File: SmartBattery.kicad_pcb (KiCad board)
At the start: 4 copper layers, 100 x 80 mm, 433 parts, among them J1 USB_C_Receptacle_USB2.0, J10 JST 2P-1.0, J11 JST 2P-1.0, J12 Conn_02x05_Odd_Even, J13 Conn_01x03_Male, J15 USB_C_Receptacle_USB2.0, J2 ST-USB-003A, J3 JACK-C-PC-10A-RA(R), J4 JST 2P-1.0, J5 JST 2P-1.0, J6 JST 2P-1.0, J7 JST 2P-1.0, J8 JST 2P-1.0, J9 JST 2P-1.0, Q1 VBA2625, Q10 AON7400A, Q11 AON7400A, Q12 BSC067N06LS3, Q13 BSC067N06LS3, Q14 2n7002K, Q15 VBA2625, Q16 VBA2625, Q17 VBA2625, Q18 VBA2625, Q19 VBA2625, Q2 2n7002K, Q20 VBA2625, Q21 2n7002K, Q22 AO3401A, Q23 VBA2625, Q24 VBA2625, Q25 2n7002K, Q26 VBA2625, Q27 VBA2625, Q3 AON7400A, Q4 AON7400A, Q5 AON7400A, Q6 AON7400A, Q7 2n7002K, Q8 AON7400A, Q9 AON7400A, SW1 SW_Push, SW2 SW_Push, SW3 SW_Push, SW4 SW_Push, U1 BQ25703ARSNR, U10 ESP32-WROOM-32U, U11 STUSB4500, U12 STUSB4700, U13 TPS2511DGNR, U14 HT7533-1, U15 LMR14030SDDAR, U2 BQ294706DSGR, U3 ITV4030, U4 BQ40Z50, U5 LM5175PWPR, U6 STM32F730R8T6, U7 LY68L6400SLIT, U8 LMR14030SDDAR, U9 FS35ND01G-S1Y2QWFI000, Y1 Q13FC1350000400, Y2 Crystal_GND24

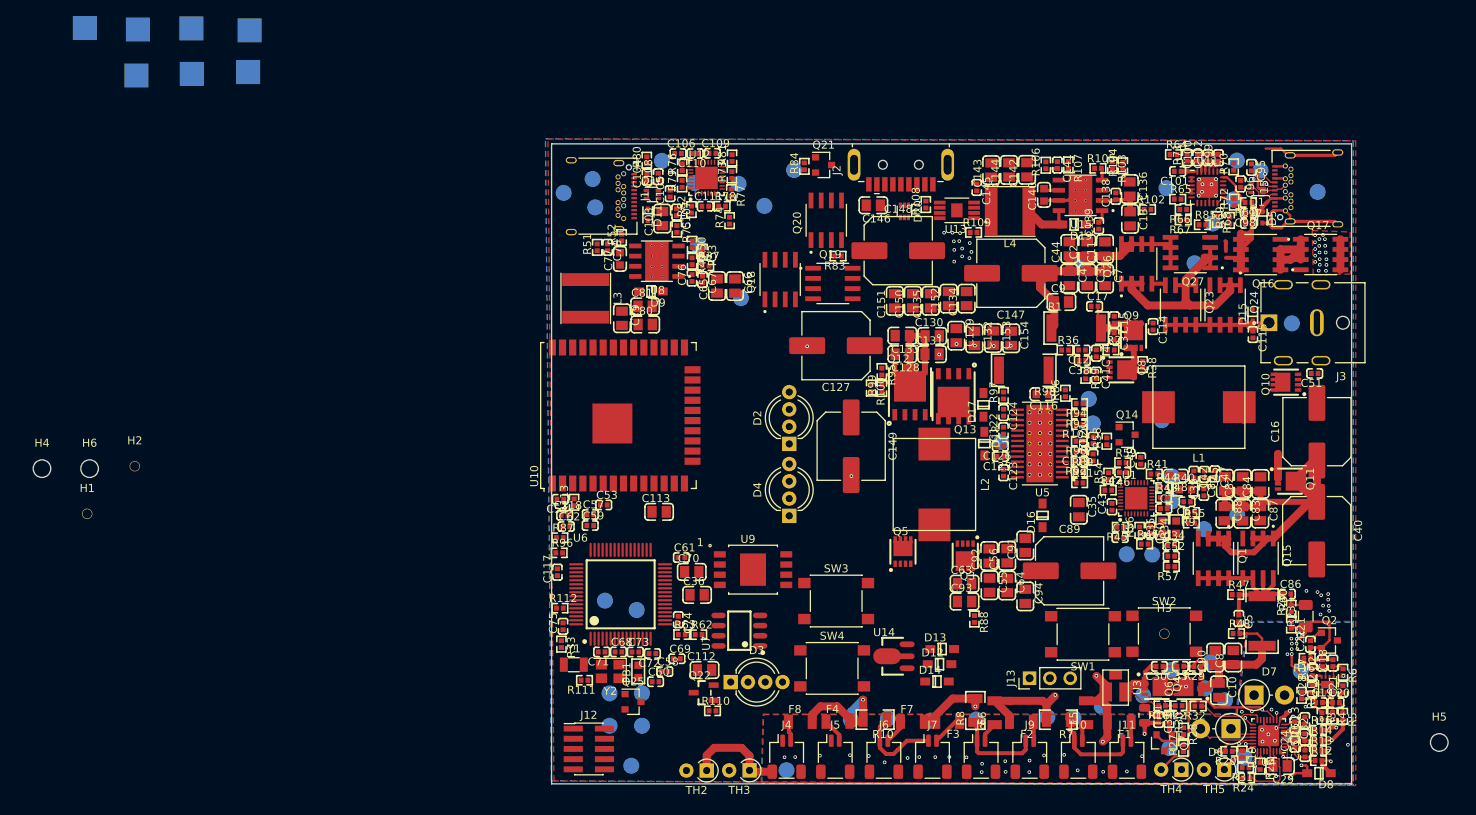
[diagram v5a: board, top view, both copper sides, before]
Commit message: Almost connected MCU + ESP32 added leds addedd uart usb cleaned up type-c I/O -- STILL NEED TO level shift I2C
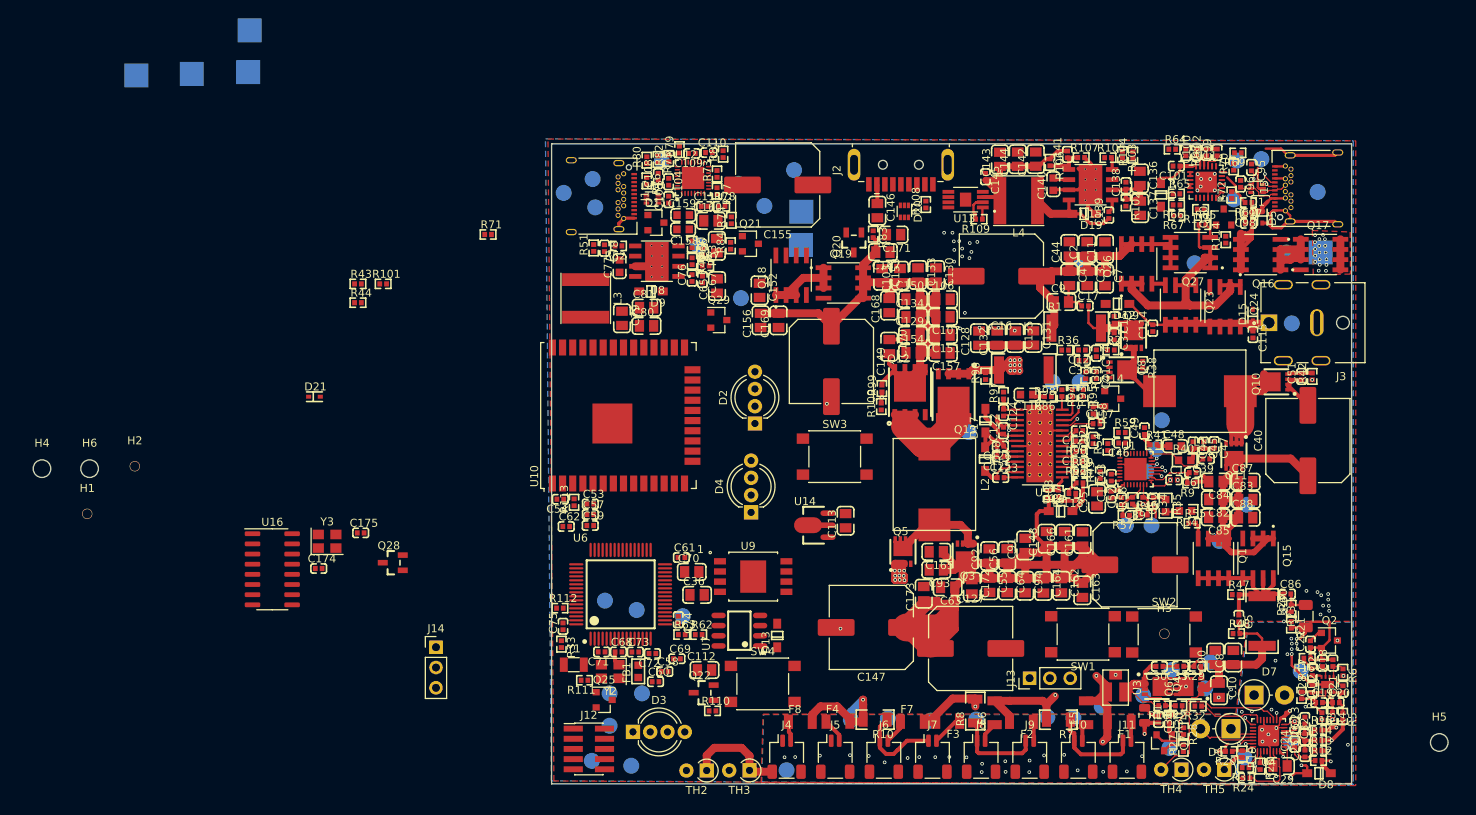
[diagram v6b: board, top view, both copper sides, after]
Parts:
- removed TP32, TP38: TestPoint, TestPoint:TestPoint_Pad_D2.0mm
- added C155: 470u, Capacitor_SMD:C_Elec_10x10.2, F.Cu at (28.3, 5.14)
- added C156: 10u 50v, lc_lib:0805_C, F.Cu at (26.1, 22.1)
- added C157: 10u 50v, lc_lib:0805_C, F.Cu at (48.9, 26.1)
- added C158: 1uF 50v, lc_lib:0603_C, F.Cu at (16.4, 10.7)
- added C159: 1uF 50v, lc_lib:0603_C, F.Cu at (16.5, 8.90)
- added C160: 10u 50v, lc_lib:0805_C, F.Cu at (19.9, 9.62)
- added C161: 22u, lc_lib:0805_C, F.Cu at (66.4, 49.4)
- added C162: 22u, lc_lib:0805_C, F.Cu at (63.7, 55.2)
- added C163: 22u, lc_lib:0805_C, F.Cu at (66.3, 55.8)
- added C164: 22u, lc_lib:0805_C, F.Cu at (61.5, 55.3)
- added C165: 22u, lc_lib:0805_C, F.Cu at (48.1, 51.0)
- added C166: 22u, lc_lib:0805_C, F.Cu at (64.1, 49.4)
- added C167: 10u 50v, lc_lib:0805_C, F.Cu at (41.4, 13.5)
- added C168: 10u 50v, lc_lib:0805_C, F.Cu at (42.2, 20.2)
- added C169: 10u 50v, lc_lib:0805_C, F.Cu at (28.4, 22.1)
- added C170: 10u 50v, lc_lib:0805_C, F.Cu at (42.2, 25.4)
- added C171: 10u 50v, lc_lib:0805_C, F.Cu at (42.8, 11.3)
- added C172: 22u, lc_lib:0805_C, F.Cu at (52.5, 55.4)
- added C173: 22u, lc_lib:0805_C, F.Cu at (46.5, 56.2)
- added C174: 12pF 0402, lc_lib:0402_C, F.Cu at (-29.1, 53.1)
- added C175: 12pF 0402, lc_lib:0402_C, F.Cu at (-23.9, 48.6)
- added D21: PESD24VS1UB-N, lc_lib:SOD-523, F.Cu at (-29.6, 31.6)
- added J14: Conn_01x03_Male, Connector_PinHeader_2.54mm:PinHeader_1x03_P2.54mm_Vertical, F.Cu at (-14.4, 62.9)
- added Q28: LBSS84LT1G, lc_lib:SOT-23(SOT-23-3), F.Cu at (-19.9, 52.4)
- added Q29: 2N7002, Package_TO_SOT_SMD:SOT-23, F.Cu at (20.9, 22.0)
- added Q30: 2N7002, Package_TO_SOT_SMD:SOT-23, F.Cu at (84.0, 9.15)
- added R114: 1k, lc_lib:0402_R, F.Cu at (84.3, 12.0)
- added R115: 10k, lc_lib:0402_R, F.Cu at (81.1, 8.18)
- added U16: CH340G, Package_SO:SOIC-16_3.9x9.9mm_P1.27mm, F.Cu at (-34.9, 53.2)
- added Y3: 12MHz, Crystal:Crystal_SMD_3225-4Pin_3.2x2.5mm, F.Cu at (-28.1, 49.7)
- C103: value 10u -> 10u 50v
- C106, C107: value 1uF 25v -> 10u 50v; footprint lc_lib:0402_C -> lc_lib:0805_C
- C127, C147, C149, C16, C40, C89: value 220u -> 470u; footprint Capacitor_SMD:C_Elec_8x10.2 -> Capacitor_SMD:C_Elec_10x10.2
- C128, C129, C130, C131, C132, C133, C134, C135, C150, C151, C152, C153, C154: value 22u -> 10u 50v
- C148: value 220u -> 22u; footprint Capacitor_SMD:C_Elec_8x10.2 -> lc_lib:0805_C
- D11: value PESD24VS1UB-N -> NUP3105LT1G; footprint lc_lib:SOD-523 -> Package_TO_SOT_SMD:SOT-23
- Q20: value VBA2625 -> LBSS84LT1G; footprint SmartBattery:SOIC127P600X175-8N -> lc_lib:SOT-23(SOT-23-3)
- Q21: value 2n7002K -> 2N7002
- R101: value ?? -> 10k
- R43: value 0 -> 1k
- Y2: value Crystal_GND24 -> 24MHz
- moved TP49 143.9 mm to (96.1, 13.6)
- moved R43 104.2 mm to (-24.2, 17.5)
- moved R44 103.4 mm to (-24.2, 19.9)
- moved TP55 93.5 mm to (31.2, 12.6)
- moved R101 88.8 mm to (-21.1, 17.5), turned to 0 degrees
- moved R71 87.9 mm to (-7.94, 11.3), turned to 0 degrees
- moved TP50 86.0 mm to (31.2, 8.49)
- moved C117 69.9 mm to (68.1, 35.0), turned to 0 degrees
- moved TP15 68.6 mm to (16.4, 59.0)
- moved D14 67.0 mm to (76.2, 6.38), turned to 270 degrees
- moved C118 63.5 mm to (65.1, 43.7), turned to 180 degrees
- moved R87 61.3 mm to (62.0, 43.7), turned to 270 degrees
- moved R96 57.7 mm to (54.2, 29.0), turned to 90 degrees
- moved D12 50.2 mm to (70.7, 20.0), turned to 180 degrees
- moved C147 47.6 mm to (40.0, 60.5)
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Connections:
- net /Battery connection and protection/BATT_PACK_P renamed /BATT_PACK_P
- C103 pad 1: GND -> /Type_C_Output/OUTPUT_TYPEC_PWR
- C103 pad 2: Net-(C103-Pad2) -> GND
- C106 pad 1: GND -> /Type_C_Output/OUTPUT_TYPEC_PWR
- C106 pad 2: Net-(C103-Pad2) -> GND
- C107 pad 1: Net-(C103-Pad2) -> GND
- C107 pad 2: GND -> /Type_C_Output/OUTPUT_TYPEC_PWR
- C111 pad 1: /Type_C_Output/OUTPUT_TYPEC_VCON -> Net-(C111-Pad1)
- C127 pad 1: /Type_C_Output/OUTPUT_TYPEC_PWR -> /Charger/VSYS
- C129 pad 1: /Type_C_Output/OUTPUT_TYPEC_PWR -> GND
- C129 pad 2: GND -> /Type_C_Output/OUTPUT_TYPEC_PWR
- C130 pad 1: /Type_C_Output/OUTPUT_TYPEC_PWR -> GND
- C130 pad 2: GND -> /Type_C_Output/OUTPUT_TYPEC_PWR
- C131 pad 1: /Type_C_Output/OUTPUT_TYPEC_PWR -> GND
- C131 pad 2: GND -> /Type_C_Output/OUTPUT_TYPEC_PWR
- C133 pad 1: /Type_C_Output/OUTPUT_TYPEC_PWR -> GND
- C133 pad 2: GND -> /Type_C_Output/OUTPUT_TYPEC_PWR
- C134 pad 1: /Type_C_Output/OUTPUT_TYPEC_PWR -> GND
- C134 pad 2: GND -> /Type_C_Output/OUTPUT_TYPEC_PWR
- C135 pad 1: /Type_C_Output/OUTPUT_TYPEC_PWR -> GND
- C135 pad 2: GND -> /Type_C_Output/OUTPUT_TYPEC_PWR
- C147 pad 1: /Charger/ADAPTER_IN -> /Charger/VSYS
- C148 pad 1: /Type_C_Output/OUTPUT_TYPEC_PWR -> /Charger/VSYS
- C150 pad 1: /Type_C_Output/OUTPUT_TYPEC_PWR -> GND
- C150 pad 2: GND -> /Type_C_Output/OUTPUT_TYPEC_PWR
- C151 pad 1: /Type_C_Output/OUTPUT_TYPEC_PWR -> GND
- C151 pad 2: GND -> /Type_C_Output/OUTPUT_TYPEC_PWR
- C152 pad 1: /Type_C_Output/OUTPUT_TYPEC_PWR -> GND
- C152 pad 2: GND -> /Type_C_Output/OUTPUT_TYPEC_PWR
- C153 pad 1: /Type_C_Output/OUTPUT_TYPEC_PWR -> GND
- C153 pad 2: GND -> /Type_C_Output/OUTPUT_TYPEC_PWR
- C154 pad 1: /Type_C_Output/OUTPUT_TYPEC_PWR -> GND
- C154 pad 2: GND -> /Type_C_Output/OUTPUT_TYPEC_PWR
- C16 pad 1: /Charger/VSYS -> /Charger/ADAPTER_IN
- D11 pad 1: GND -> Net-(C158-Pad2)
- D11 pad 2: Net-(C103-Pad2) -> Net-(C158-Pad2)
- J1 pad A4: Net-(C103-Pad2) -> Net-(C158-Pad2)
- J1 pad A9: Net-(C103-Pad2) -> Net-(C158-Pad2)
- J1 pad B4: Net-(C103-Pad2) -> Net-(C158-Pad2)
- J1 pad B9: Net-(C103-Pad2) -> Net-(C158-Pad2)
- Q1 pad 2: /Charger/VSYS -> (no net)
- Q1 pad 3: /Charger/VSYS -> (no net)
- Q1 pad 5: Net-(C5-Pad1) -> (no net)
- Q1 pad 6: Net-(C5-Pad1) -> (no net)
- Q1 pad 7: Net-(C5-Pad1) -> (no net)
- Q15 pad 2: /Charger/VSYS -> (no net)
- Q15 pad 3: /Charger/VSYS -> (no net)
- Q15 pad 5: Net-(C5-Pad1) -> (no net)
- Q15 pad 6: Net-(C5-Pad1) -> (no net)
- Q15 pad 7: Net-(C5-Pad1) -> (no net)
- Q16 pad 2: Net-(Q16-Pad1) -> (no net)
- Q16 pad 3: Net-(Q16-Pad1) -> (no net)
- Q16 pad 5: /type_c_input/INPUT_TYPEC_VBUS_RAW -> (no net)
- Q16 pad 6: /type_c_input/INPUT_TYPEC_VBUS_RAW -> (no net)
- Q16 pad 7: /type_c_input/INPUT_TYPEC_VBUS_RAW -> (no net)
- Q17 pad 2: Net-(Q16-Pad1) -> (no net)
- Q17 pad 3: Net-(Q16-Pad1) -> (no net)
- Q17 pad 5: /Charger/ADAPTER_IN -> (no net)
- Q17 pad 6: /Charger/ADAPTER_IN -> (no net)
- Q17 pad 7: /Charger/ADAPTER_IN -> (no net)
- Q18 pad 2: Net-(Q18-Pad1) -> (no net)
- Q18 pad 3: Net-(Q18-Pad1) -> (no net)
- Q18 pad 5: Net-(C103-Pad2) -> (no net)
- Q18 pad 6: Net-(C103-Pad2) -> (no net)
- Q18 pad 7: Net-(C103-Pad2) -> (no net)
- Q18 pad 8: Net-(C103-Pad2) -> Net-(C158-Pad2)
- Q19 pad 2: Net-(Q18-Pad1) -> (no net)
- Q19 pad 3: Net-(Q18-Pad1) -> (no net)
- Q19 pad 5: /Type_C_Output/OUTPUT_TYPEC_PWR -> (no net)
- Q19 pad 6: /Type_C_Output/OUTPUT_TYPEC_PWR -> (no net)
- Q19 pad 7: /Type_C_Output/OUTPUT_TYPEC_PWR -> (no net)
- Q20 pad 2: /Type_C_Output/OUTPUT_TYPEC_PWR -> (no net)
- Q20 pad 3: /Type_C_Output/OUTPUT_TYPEC_PWR -> (no net)
- Q21 pad 1: /Type_C_Output/OUTPUT_TYPEC_VCON -> /Type_C_Output/OUTPUT_TYPEC_MCUPWR
- Q23 pad 2: Net-(Q23-Pad1) -> (no net)
- Q23 pad 3: Net-(Q23-Pad1) -> (no net)
- Q23 pad 5: /Barrel_Jack_Input/BARREL_RAW -> (no net)
- Q23 pad 6: /Barrel_Jack_Input/BARREL_RAW -> (no net)
- Q23 pad 7: /Barrel_Jack_Input/BARREL_RAW -> (no net)
- Q24 pad 2: Net-(Q23-Pad1) -> (no net)
- Q24 pad 3: Net-(Q23-Pad1) -> (no net)
- Q24 pad 5: /Barrel_Jack_Input/BARREL_RAW -> (no net)
- Q24 pad 6: /Barrel_Jack_Input/BARREL_RAW -> (no net)
- Q24 pad 7: /Barrel_Jack_Input/BARREL_RAW -> (no net)
- Q26 pad 2: Net-(Q23-Pad1) -> (no net)
- Q26 pad 3: Net-(Q23-Pad1) -> (no net)
- Q26 pad 5: /Charger/ADAPTER_IN -> (no net)
- Q26 pad 6: /Charger/ADAPTER_IN -> (no net)
- Q26 pad 7: /Charger/ADAPTER_IN -> (no net)
- Q27 pad 2: Net-(Q23-Pad1) -> (no net)
- Q27 pad 3: Net-(Q23-Pad1) -> (no net)
- Q27 pad 5: /Charger/ADAPTER_IN -> (no net)
- Q27 pad 6: /Charger/ADAPTER_IN -> (no net)
- Q27 pad 7: /Charger/ADAPTER_IN -> (no net)
- R101 pad 1: /OutputStage/VOLTAGE_CONTROL -> Net-(Q29-Pad1)
- R101 pad 2: Net-(R100-Pad2) -> Net-(C158-Pad2)
- R32 pad 2: /Battery connection and protection/BATT_SHUTDOWN_N -> /BATT_SHUTDOWN_N
- R43 pad 1: Net-(R43-Pad1) -> GND
- R43 pad 2: Net-(R43-Pad2) -> Net-(Q29-Pad2)
- R44 pad 1: Net-(R44-Pad1) -> /Type_C_Output/OUTPUT_TYPEC_MCUPWR
- R44 pad 2: Net-(R44-Pad2) -> Net-(C111-Pad1)
- R71 pad 1: /type_c_input/2v7_local -> /Type_C_Output/OUTPUT_TYPEC_RESET
- R71 pad 2: /type_c_input/INPUT_TYPEC_AWAKE -> GND
- R74 pad 1: Net-(C103-Pad2) -> Net-(C158-Pad2)
- R76 pad 2: Net-(C103-Pad2) -> Net-(C158-Pad2)
- R84 pad 2: /Type_C_Output/OUTPUT_TYPEC_VCON -> /Type_C_Output/OUTPUT_TYPEC_MCUPWR
- TP15 pad 1: /Battery connection and protection/BATT_INT -> /BATT_INT_N
- TP16 pad 1: /Battery connection and protection/BATT_SMB_C -> /BATT_SMB_C
- TP17 pad 1: /Battery connection and protection/BATT_SMB_D -> /BATT_SMB_D
- TP25 pad 1: Net-(R43-Pad1) -> Net-(TP25-Pad1)
- TP26 pad 1: Net-(R44-Pad2) -> Net-(TP26-Pad1)
- TP37 pad 1: Net-(C103-Pad2) -> Net-(C158-Pad2)
- U1 pad 14: Net-(R43-Pad2) -> Net-(TP25-Pad1)
- U1 pad 15: Net-(R44-Pad1) -> Net-(TP26-Pad1)
- U12 pad 19: Net-(TP38-Pad1) -> Net-(Q29-Pad1)
- U12 pad 3: /Type_C_Output/OUTPUT_TYPEC_VCON -> Net-(C111-Pad1)
- U15 pad 10: (no net) -> GND
- U15 pad 11: (no net) -> GND
- U15 pad 12: (no net) -> GND
- U15 pad 13: (no net) -> GND
- U15 pad 14: (no net) -> GND
- U15 pad 15: (no net) -> GND
- U15 pad 16: (no net) -> GND
- U15 pad 17: (no net) -> GND
- U4 pad 15: /Battery connection and protection/BATT_INT -> /BATT_INT_N
- U4 pad 18: /Battery connection and protection/BATT_SMB_D -> /BATT_SMB_D
- U4 pad 19: /Battery connection and protection/BATT_SMB_C -> /BATT_SMB_C
- U5 pad 30: (no net) -> GND
- U5 pad 31: (no net) -> GND
- U5 pad 32: (no net) -> GND
- U5 pad 33: (no net) -> GND
- U5 pad 34: (no net) -> GND
- U5 pad 35: (no net) -> GND
- U5 pad 36: (no net) -> GND
- U5 pad 37: (no net) -> GND
- U5 pad 38: (no net) -> GND
- U5 pad 39: (no net) -> GND
- U5 pad 40: (no net) -> GND
- U5 pad 41: (no net) -> GND
- U5 pad 42: (no net) -> GND
- U5 pad 43: (no net) -> GND
- U5 pad 44: (no net) -> GND
- U5 pad 45: (no net) -> GND
- U5 pad 46: (no net) -> GND
- U5 pad 47: (no net) -> GND
- U5 pad 48: (no net) -> GND
- U5 pad 49: (no net) -> GND
- U5 pad 50: (no net) -> GND
- U6 pad 33: Net-(U6-Pad33) -> /MCU/SPI2_NSS
- U6 pad 57: /MCU/I2C1_SMBA -> /BATT_INT_N
- U6 pad 59: /MCU/I2C1_SDA -> /BATT_SMB_D
- U6 pad 61: /MCU/I2C1_SCL -> /BATT_SMB_C
- U6 pad 62: Net-(U6-Pad62) -> /BATT_SHUTDOWN_N
- U8 pad 10: (no net) -> GND
- U8 pad 11: (no net) -> GND
- U8 pad 12: (no net) -> GND
- U8 pad 13: (no net) -> GND
- U8 pad 14: (no net) -> GND
- U8 pad 15: (no net) -> GND
- U8 pad 16: (no net) -> GND
- U8 pad 17: (no net) -> GND
- U9 pad 1: Net-(U9-Pad1) -> /MCU/SPI2_NSS
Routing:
- net /Charger/VSYS: track 56.9 -> 194.3 mm
- net /Type_C_Output/OUTPUT_TYPEC_PWR: track 26.0 -> 128.0 mm, vias 0 -> 1
- net GND: track 50.6 -> 109.8 mm, vias 36 -> 46
- net Net-(Q13-Pad1): track 0.00 -> 52.4 mm, vias 0 -> 18
- net Net-(Q2-Pad3): track 0.00 -> 32.9 mm, vias 0 -> 2
- net Net-(R100-Pad2): track 0.00 -> 29.2 mm, vias 0 -> 2
- net Net-(TH4-Pad2): track 48.6 -> 22.3 mm, vias 1 -> 0
- net /Peripheral_3p3v/5v0: track 0.73 -> 22.3 mm
- net /Barrel_Jack_Input/BARREL_RAW: track 19.5 -> 38.2 mm
- net /OutputStage/SW2: track 0.00 -> 18.4 mm
- net Net-(C46-Pad1): track 4.09 -> 22.2 mm
- net Net-(C32-Pad1): track 1.44 -> 17.2 mm, vias 0 -> 2
- net Net-(C32-Pad2): track 1.43 -> 17.1 mm, vias 0 -> 2
- net /OutputStage/SW1: track 0.00 -> 14.3 mm
- net Net-(Q18-Pad1): track 0.00 -> 10.6 mm
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
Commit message: lots of GPIO connectivity changes. fixed no PD on input fixed CH340G leakage. can otherwise power from GPIO. added fet for powering VCONN from 3v/5v NEED TO ADD OVERCURRENT
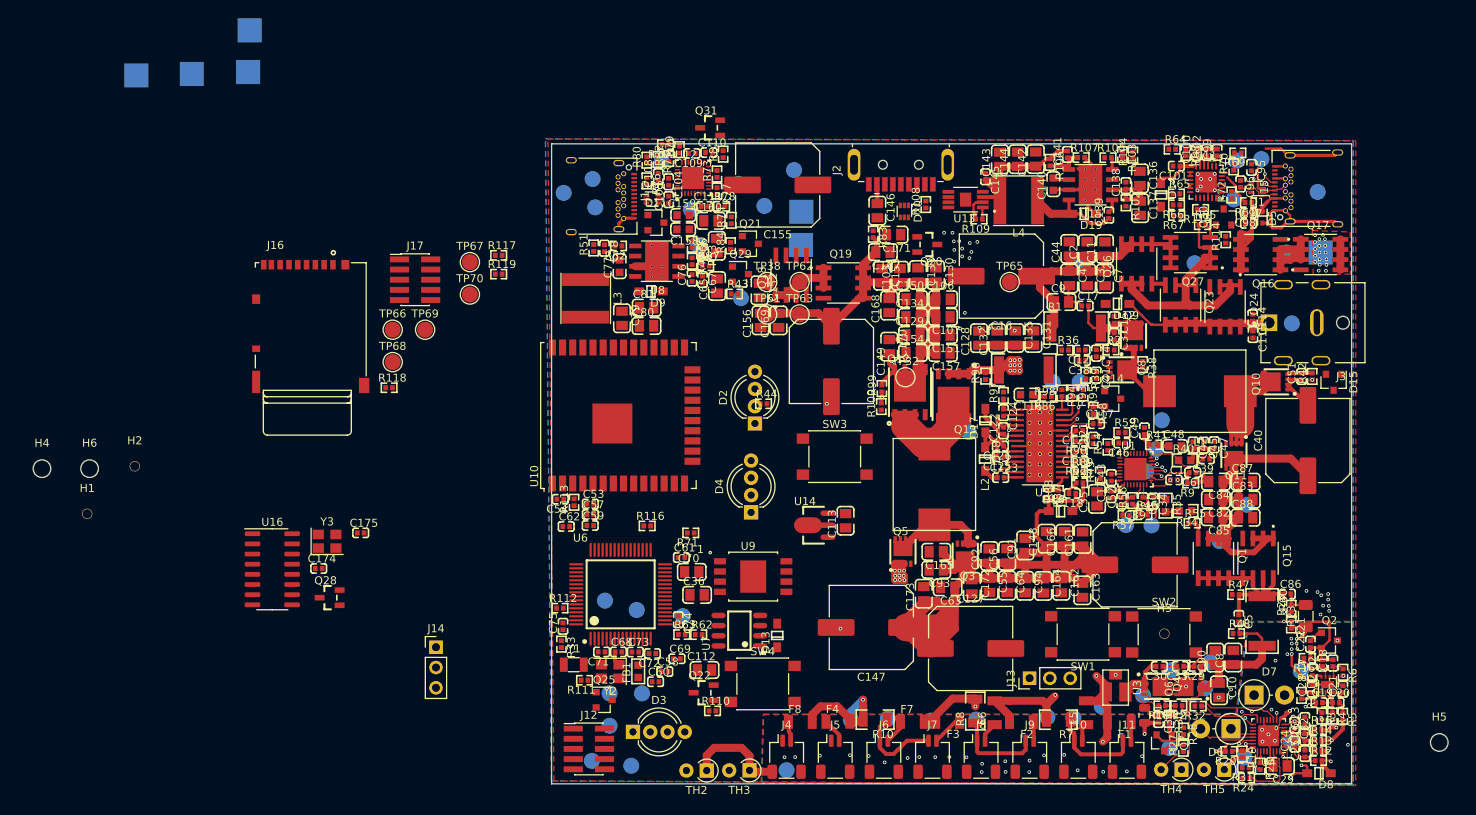
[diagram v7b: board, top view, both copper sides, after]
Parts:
- removed D21: PESD24VS1UB-N, lc_lib:SOD-523
- added J16: DM3AT-SF-PEJM5, SmartBattery:HRS_DM3AT-SF-PEJM5, F.Cu at (-30.5, 15.1)
- added J17: Conn_02x05_Odd_Even, Connector_PinHeader_1.27mm:PinHeader_2x05_P1.27mm_Vertical_SMD, F.Cu at (-17.1, 17.0)
- added Q31: LBSS84LT1G, lc_lib:SOT-23(SOT-23-3), F.Cu at (19.8, -2.00)
- added R116: 100k, lc_lib:0402_R, F.Cu at (11.9, 47.8)
- added R117: 100, lc_lib:0402_R, F.Cu at (-6.61, 13.9)
- added R118: 100, lc_lib:0402_R, F.Cu at (-20.3, 30.5)
- added R119: 100, lc_lib:0402_R, F.Cu at (-6.61, 16.3)
- added TP32: TestPoint, TestPoint:TestPoint_Pad_D2.0mm, F.Cu at (44.2, 29.2)
- added TP38: TestPoint, TestPoint:TestPoint_Pad_D2.0mm, F.Cu at (26.9, 17.3)
- added TP61: TestPoint, TestPoint:TestPoint_Pad_D2.0mm, F.Cu at (26.9, 21.3)
- added TP62: TestPoint, TestPoint:TestPoint_Pad_D2.0mm, F.Cu at (31.0, 17.3)
- added TP63: TestPoint, TestPoint:TestPoint_Pad_D2.0mm, F.Cu at (31.0, 21.3)
- added TP64: TestPoint, TestPoint:TestPoint_Pad_D2.0mm, B.Cu at (17.4, 8.19)
- added TP65: TestPoint, TestPoint:TestPoint_Pad_D2.0mm, F.Cu at (57.3, 17.3)
- added TP66: TestPoint, TestPoint:TestPoint_Pad_D2.0mm, F.Cu at (-19.9, 23.2)
- added TP67: TestPoint, TestPoint:TestPoint_Pad_D2.0mm, F.Cu at (-10.2, 14.8)
- added TP68: TestPoint, TestPoint:TestPoint_Pad_D2.0mm, F.Cu at (-19.9, 27.3)
- added TP69: TestPoint, TestPoint:TestPoint_Pad_D2.0mm, F.Cu at (-15.8, 23.2)
- added TP70: TestPoint, TestPoint:TestPoint_Pad_D2.0mm, F.Cu at (-10.2, 18.8)
- C114, C115: value 1uF 25v -> 1uF 50v
- D15: value PESD24VS1UB-N -> NUP3105LT1G; footprint lc_lib:SOD-523 -> Package_TO_SOT_SMD:SOT-23
- R44: value 0 -> 100k
- moved R44 52.3 mm to (26.5, 32.5)
- moved R43 47.1 mm to (22.9, 18.8)
- moved R71 45.1 mm to (17.4, 48.6), turned to 180 degrees
- moved R101 39.4 mm to (14.2, 0.10), turned to 180 degrees
- moved D15 13.1 mm to (97.8, 29.8), turned to 270 degrees
- moved C114 12.6 mm to (87.6, 21.7), turned to 270 degrees
- moved Q20 9.18 mm to (47.0, 12.6), turned to 180 degrees
- moved Q28 9.03 mm to (-27.8, 56.7)
- moved Q29 6.35 mm to (23.6, 16.3)
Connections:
- net /Output_TYPEA/5v_ENABLE renamed /5V_ENABLE
- net /Type_C_Output/OUTPUT_TYPEC_ALERT_N renamed /OUTPUT_ALERT_N
- net /Type_C_Output/OUTPUT_TYPEC_RESET renamed Net-(R71-Pad1)
- net /Type_C_Output/OUTPUT_TYPEC_SCL renamed /OUTPUT_TYPEC_SCL
- net /Type_C_Output/OUTPUT_TYPEC_SDA renamed /OUTPUT_TYPEC_SDA
- net /type_c_input/INPUT_TYPEC_RST renamed Net-(R65-Pad2)
- net Net-(R100-Pad2) renamed /OutputStage/VOLTAGE_CONTROL
- C111 pad 1: Net-(C111-Pad1) -> /Type_C_Output/VCONN
- C160 pad 2: Net-(C160-Pad2) -> Net-(C158-Pad2)
- D1 pad 1: /type_c_input/INPUT_DP -> /INPUT_USB_DM
- D1 pad 3: /type_c_input/INPUT_DM -> /INPUT_USB_DM
- D10 pad 1: /Type_C_Output/OUTPUT_DP -> /OUTPUT_USB_DM
- D10 pad 3: /Type_C_Output/OUTPUT_DM -> /OUTPUT_USB_DM
- D15 pad 1: GND -> /Barrel_Jack_Input/BARREL_RAW
- D3 pad 2: Net-(D3-Pad2) -> +3.3VP
- D4 pad 2: Net-(D4-Pad2) -> +3.3VP
- J1 pad A6: /Type_C_Output/OUTPUT_DP -> /OUTPUT_USB_DM
- J1 pad A7: /Type_C_Output/OUTPUT_DM -> /OUTPUT_USB_DM
- J1 pad B6: /Type_C_Output/OUTPUT_DP -> /OUTPUT_USB_DM
- J1 pad B7: /Type_C_Output/OUTPUT_DM -> /OUTPUT_USB_DM
- J15 pad A6: /type_c_input/INPUT_DP -> /INPUT_USB_DM
- J15 pad A7: /type_c_input/INPUT_DM -> /INPUT_USB_DM
- J15 pad B6: /type_c_input/INPUT_DP -> /INPUT_USB_DM
- J15 pad B7: /type_c_input/INPUT_DM -> /INPUT_USB_DM
- Q1 pad 2: (no net) -> /Charger/VSYS
- Q1 pad 3: (no net) -> /Charger/VSYS
- Q1 pad 5: (no net) -> Net-(C5-Pad1)
- Q1 pad 6: (no net) -> Net-(C5-Pad1)
- Q1 pad 7: (no net) -> Net-(C5-Pad1)
- Q15 pad 2: (no net) -> /Charger/VSYS
- Q15 pad 3: (no net) -> /Charger/VSYS
- Q15 pad 5: (no net) -> Net-(C5-Pad1)
- Q15 pad 6: (no net) -> Net-(C5-Pad1)
- Q15 pad 7: (no net) -> Net-(C5-Pad1)
- Q16 pad 2: (no net) -> Net-(Q16-Pad1)
- Q16 pad 3: (no net) -> Net-(Q16-Pad1)
- Q16 pad 5: (no net) -> /type_c_input/INPUT_TYPEC_VBUS_RAW
- Q16 pad 6: (no net) -> /type_c_input/INPUT_TYPEC_VBUS_RAW
- Q16 pad 7: (no net) -> /type_c_input/INPUT_TYPEC_VBUS_RAW
- Q17 pad 2: (no net) -> Net-(Q16-Pad1)
- Q17 pad 3: (no net) -> Net-(Q16-Pad1)
- Q17 pad 5: (no net) -> /Charger/ADAPTER_IN
- Q17 pad 6: (no net) -> /Charger/ADAPTER_IN
- Q17 pad 7: (no net) -> /Charger/ADAPTER_IN
- Q18 pad 2: (no net) -> Net-(Q18-Pad1)
- Q18 pad 3: (no net) -> Net-(Q18-Pad1)
- Q18 pad 5: (no net) -> Net-(C158-Pad2)
- Q18 pad 6: (no net) -> Net-(C158-Pad2)
- Q18 pad 7: (no net) -> Net-(C158-Pad2)
- Q19 pad 2: (no net) -> Net-(Q18-Pad1)
- Q19 pad 3: (no net) -> Net-(Q18-Pad1)
- Q19 pad 5: (no net) -> /Type_C_Output/OUTPUT_TYPEC_PWR
- Q19 pad 6: (no net) -> /Type_C_Output/OUTPUT_TYPEC_PWR
- Q19 pad 7: (no net) -> /Type_C_Output/OUTPUT_TYPEC_PWR
- Q20 pad 1: /Type_C_Output/OUTPUT_TYPEC_PWR -> Net-(Q20-Pad1)
- Q20 pad 2: (no net) -> /Type_C_Output/OUTPUT_TYPEC_PWR
- Q20 pad 3: (no net) -> Net-(Q20-Pad3)
- Q21 pad 1: /Type_C_Output/OUTPUT_TYPEC_MCUPWR -> /OUTPUT_TYPEC_MCUPWR
- Q21 pad 3: Net-(Q20-Pad4) -> Net-(Q20-Pad1)
- Q23 pad 2: (no net) -> Net-(Q23-Pad1)
- Q23 pad 3: (no net) -> Net-(Q23-Pad1)
- Q23 pad 5: (no net) -> /Barrel_Jack_Input/BARREL_RAW
- Q23 pad 6: (no net) -> /Barrel_Jack_Input/BARREL_RAW
- Q23 pad 7: (no net) -> /Barrel_Jack_Input/BARREL_RAW
- Q24 pad 2: (no net) -> Net-(Q23-Pad1)
- Q24 pad 3: (no net) -> Net-(Q23-Pad1)
- Q24 pad 5: (no net) -> /Barrel_Jack_Input/BARREL_RAW
- Q24 pad 6: (no net) -> /Barrel_Jack_Input/BARREL_RAW
- Q24 pad 7: (no net) -> /Barrel_Jack_Input/BARREL_RAW
- Q26 pad 2: (no net) -> Net-(Q23-Pad1)
- Q26 pad 3: (no net) -> Net-(Q23-Pad1)
- Q26 pad 5: (no net) -> /Charger/ADAPTER_IN
- Q26 pad 6: (no net) -> /Charger/ADAPTER_IN
- Q26 pad 7: (no net) -> /Charger/ADAPTER_IN
- Q27 pad 2: (no net) -> Net-(Q23-Pad1)
- Q27 pad 3: (no net) -> Net-(Q23-Pad1)
- Q27 pad 5: (no net) -> /Charger/ADAPTER_IN
- Q27 pad 6: (no net) -> /Charger/ADAPTER_IN
- Q27 pad 7: (no net) -> /Charger/ADAPTER_IN
- Q28 pad 2: (no net) -> Net-(Q28-Pad2)
- Q28 pad 3: (no net) -> Net-(Q28-Pad3)
- R44 pad 1: /Type_C_Output/OUTPUT_TYPEC_MCUPWR -> /Type_C_Output/VCONN_VOLTAGE
- R44 pad 2: Net-(C111-Pad1) -> /OUTPUT_TYPEC_MCUPWR
- R77 pad 1: /Type_C_Output/OUTPUT_TYPEC_MCUPWR -> /OUTPUT_TYPEC_MCUPWR
- R83 pad 1: Net-(Q20-Pad4) -> Net-(Q20-Pad1)
- R84 pad 2: /Type_C_Output/OUTPUT_TYPEC_MCUPWR -> /OUTPUT_TYPEC_MCUPWR
- U10 pad 10: Net-(U10-Pad10) -> Net-(D3-Pad3)
- U10 pad 11: Net-(U10-Pad11) -> Net-(D3-Pad4)
- U10 pad 12: Net-(U10-Pad12) -> Net-(D3-Pad1)
- U10 pad 13: Net-(U10-Pad13) -> /MCU/TMS
- U10 pad 14: Net-(U10-Pad14) -> /MCU/TDI
- U10 pad 16: Net-(U10-Pad16) -> /MCU/TCK
- U10 pad 23: Net-(U10-Pad23) -> /MCU/TDO
- U10 pad 27: Net-(U10-Pad27) -> /MCU/UART5_TX
- U10 pad 28: Net-(U10-Pad28) -> /MCU/UART5_RX
- U10 pad 6: Net-(U10-Pad6) -> Net-(D4-Pad4)
- U10 pad 7: Net-(U10-Pad7) -> Net-(D4-Pad1)
- U10 pad 8: Net-(U10-Pad8) -> /MCU/DET
- U10 pad 9: Net-(U10-Pad9) -> Net-(D4-Pad3)
- U12 pad 3: Net-(C111-Pad1) -> /Type_C_Output/VCONN
- U16 pad 3: Net-(Q28-Pad8) -> Net-(Q28-Pad3)
- U6 pad 42: Net-(U6-Pad42) -> /MCU/ESP32_UART_RX
- U6 pad 43: Net-(U6-Pad43) -> /MCU/ESP32_UART_TX
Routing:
- net /INPUT_USB_DM: track 0.00 -> 7.91 mm, vias 0 -> 1
- net /type_c_input/INPUT_DM: track 4.75 -> 0.00 mm, vias 1 -> 0
- net /type_c_input/INPUT_DP: track 3.16 -> 0.00 mm
